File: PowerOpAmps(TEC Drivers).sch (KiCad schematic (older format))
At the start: 23 parts, among them U301 OPA569AIDWPR, U302 OPA569AIDWPR

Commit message: pushing all changes and ports
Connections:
- net Output_of_2.5V_Reference renamed REFERENCE_2.5V
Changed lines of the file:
@@
 	1    0    0    -1
 $EndComp
-Text Label 1050 3600 0    50   ~ 0
-Output_of_2.5V_Reference
 Wire Wire Line
 	7500 5350 7600 5350
@@
 	2900 2200 3700 2200
 Wire Wire Line
-	1050 3600 3350 3600
+	1750 3600 3350 3600
 Text Label 1100 2500 0    50   ~ 0
 Enable_Signal_from_Arduino_D5
@@
 	0    1    -1   0
 $EndComp
-Text HLabel 9450 2700 2    50   Input ~ 0
-4.2V_Power_Supply
+Text GLabel 9450 2700 2    50   Input ~ 0
+4.2V
+Text GLabel 1750 3600 0    50   Input ~ 0
+REFERENCE_2.5V
 $EndSCHEMATC

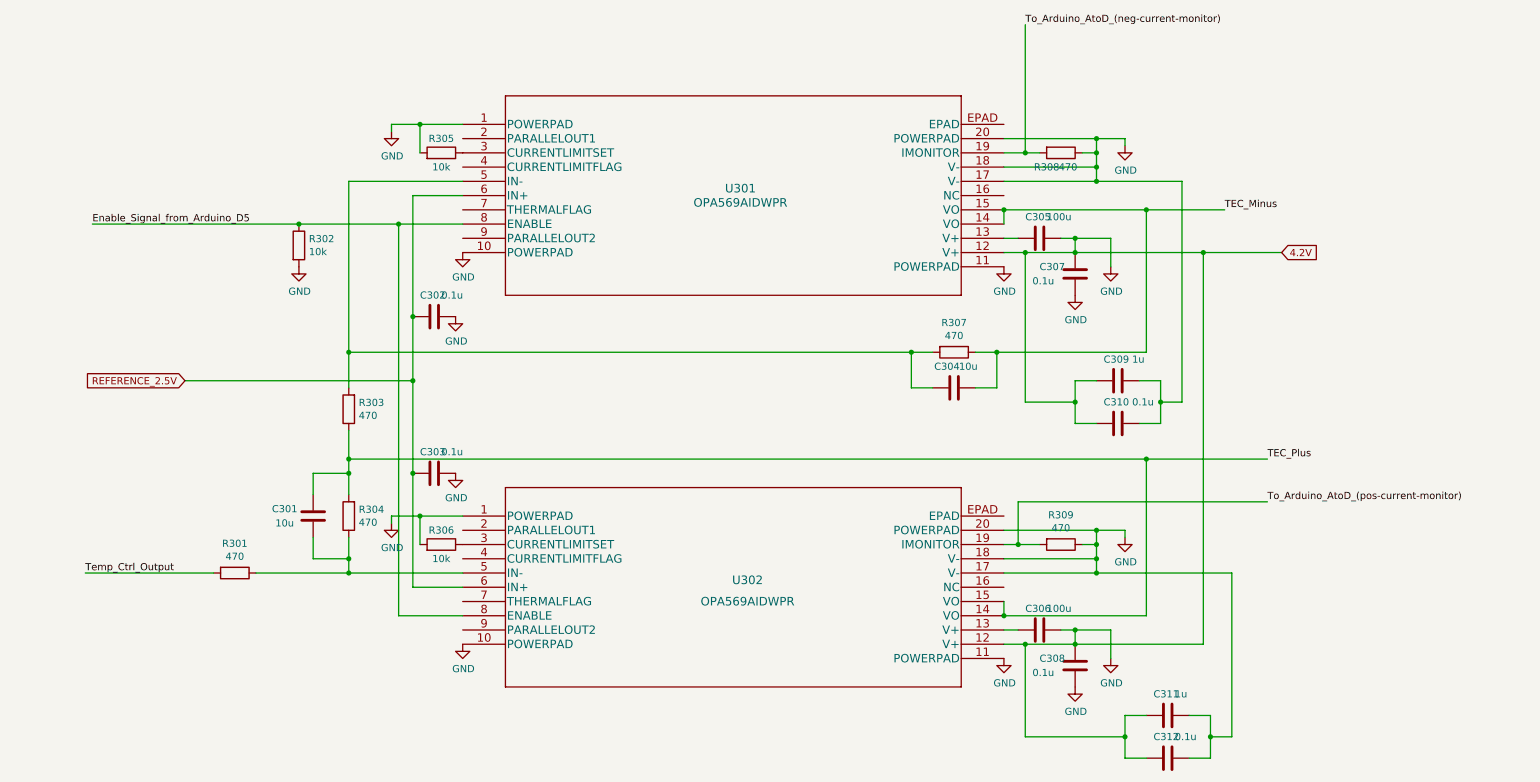
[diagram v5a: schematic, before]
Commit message: add thermal control output
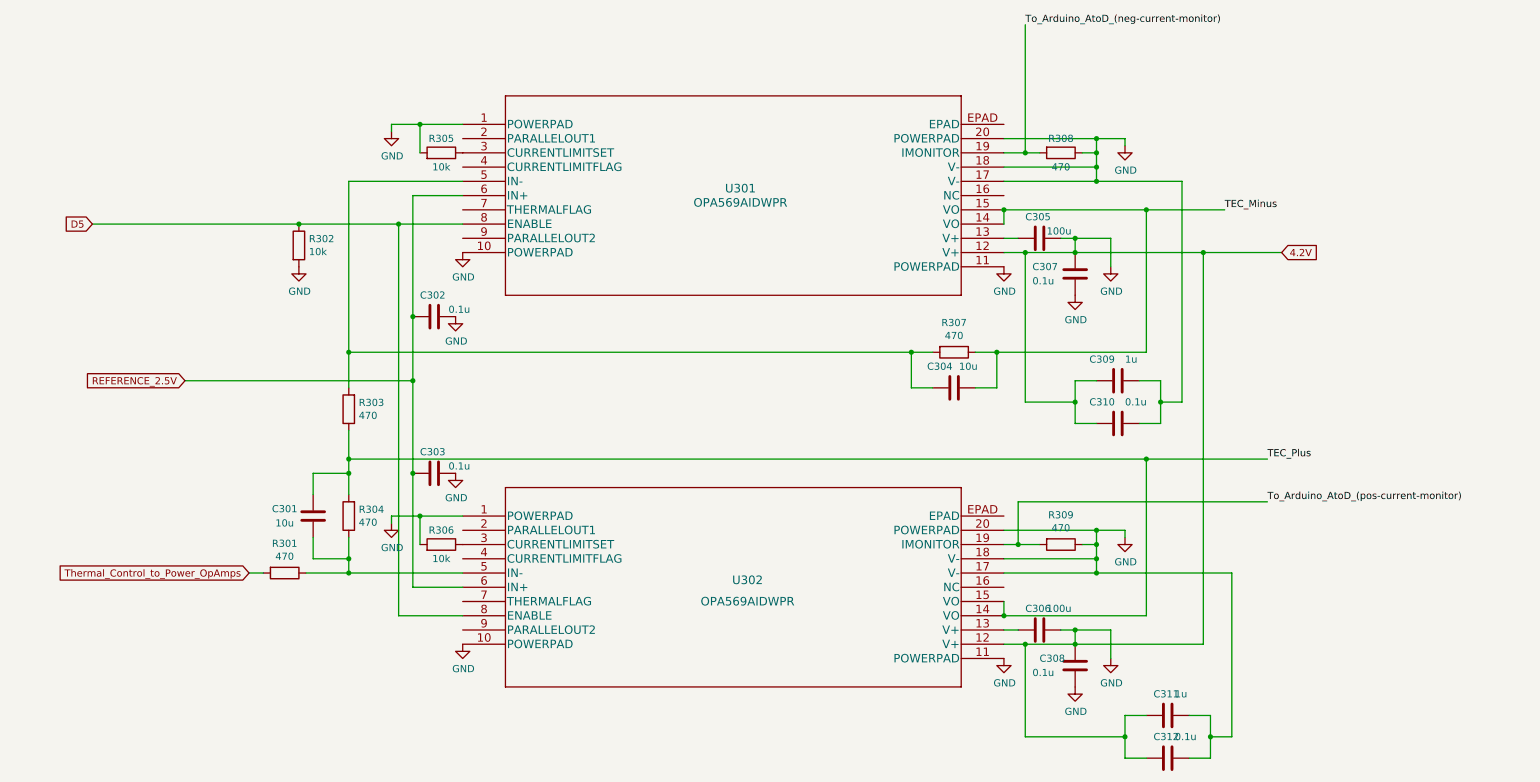
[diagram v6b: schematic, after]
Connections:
- net Enable_Signal_from_Arduino_D5 renamed D5
- net Temp_Ctrl_Output renamed Thermal_Control_to_Power_OpAmps
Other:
- moved on the sheet: R301
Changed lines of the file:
@@
 U 1 1 60C9D180
 P 7900 2000
-F 0 "R308" V 8000 1900 50  0000 C CNN
-F 1 "470" V 8000 2050 50  0000 C CNN
+F 0 "R308" V 7800 2000 50  0000 C CNN
+F 1 "470" V 8000 2000 50  0000 C CNN
 F 2 "Resistor_SMD:R_0402_1005Metric" V 7830 2000 50  0001 C CNN
 F 3 "~" H 7900 2000 50  0001 C CNN
@@
 U 1 1 60C9E72B
 P 8000 2850
-F 0 "C307" H 7750 2900 50  0000 L CNN
+F 0 "C307" H 7700 2900 50  0000 L CNN
 F 1 "0.1u" H 7700 2800 50  0000 L CNN
 F 2 "Capacitor_SMD:C_0402_1005Metric" H 8038 2700 50  0001 C CNN
@@
 P 7750 2600
 F 0 "C305" V 7600 2500 50  0000 L CNN
-F 1 "100u" V 7600 2650 50  0000 L CNN
+F 1 "100u" V 7700 2650 50  0000 L CNN
 F 2 "Capacitor_SMD:C_0402_1005Metric" H 7788 2450 50  0001 C CNN
 F 3 "~" H 7750 2600 50  0001 C CNN
@@
 U 1 1 60CADB61
 P 7150 3650
-F 0 "C304" V 7000 3600 50  0000 C CNN
+F 0 "C304" V 7000 3550 50  0000 C CNN
 F 1 "10u" V 7000 3750 50  0000 C CNN
 F 2 "Capacitor_SMD:C_0402_1005Metric" H 7188 3500 50  0001 C CNN
@@
 Wire Wire Line
 	2900 4850 2900 4950
-Wire Wire Line
-	2900 4950 2250 4950
-Connection ~ 2900 4950
 $Comp
 L Device:R R301
 U 1 1 60CB799D
-P 2100 4950
-F 0 "R301" V 1893 4950 50  0000 C CNN
-F 1 "470" V 1984 4950 50  0000 C CNN
-F 2 "Resistor_SMD:R_0402_1005Metric" V 2030 4950 50  0001 C CNN
-F 3 "~" H 2100 4950 50  0001 C CNN
-	1    2100 4950
-	0    1    1    0
-$EndComp
-Wire Wire Line
-	1950 4950 1050 4950
-Text Label 1050 4950 0    50   ~ 0
-Temp_Ctrl_Output
+P 2450 4950
+F 0 "R301" V 2243 4950 50  0000 C CNN
+F 1 "470" V 2334 4950 50  0000 C CNN
+F 2 "Resistor_SMD:R_0402_1005Metric" V 2380 4950 50  0001 C CNN
+F 3 "~" H 2450 4950 50  0001 C CNN
+	1    2450 4950
+	0    1    1    0
+$EndComp
 Wire Wire Line
 	3350 2300 3350 3150
@@
 P 3500 3150
 F 0 "C302" V 3350 3050 50  0000 L CNN
-F 1 "0.1u" V 3350 3200 50  0000 L CNN
+F 1 "0.1u" V 3450 3250 50  0000 L CNN
 F 2 "Capacitor_SMD:C_0402_1005Metric" H 3538 3000 50  0001 C CNN
 F 3 "~" H 3500 3150 50  0001 C CNN
@@
 P 3500 4250
 F 0 "C303" V 3350 4150 50  0000 L CNN
-F 1 "0.1u" V 3350 4300 50  0000 L CNN
+F 1 "0.1u" V 3450 4350 50  0000 L CNN
 F 2 "Capacitor_SMD:C_0402_1005Metric" H 3538 4100 50  0001 C CNN
 F 3 "~" H 3500 4250 50  0001 C CNN
@@
 Wire Wire Line
 	1750 3600 3350 3600
-Text Label 1100 2500 0    50   ~ 0
-Enable_Signal_from_Arduino_D5
 $Comp
 L Device:R R302
@@
 U 1 1 60CDE792
 P 8300 3600
-F 0 "C309" V 8150 3500 50  0000 L CNN
-F 1 "1u" V 8150 3700 50  0000 L CNN
+F 0 "C309" V 8150 3400 50  0000 L CNN
+F 1 "1u" V 8150 3650 50  0000 L CNN
 F 2 "Capacitor_SMD:C_0402_1005Metric" H 8338 3450 50  0001 C CNN
 F 3 "~" H 8300 3600 50  0001 C CNN
@@
 U 1 1 60CDE79C
 P 8300 3900
-F 0 "C310" V 8150 3800 50  0000 L CNN
-F 1 "0.1u" V 8150 4000 50  0000 L CNN
+F 0 "C310" V 8150 3700 50  0000 L CNN
+F 1 "0.1u" V 8150 3950 50  0000 L CNN
 F 2 "Capacitor_SMD:C_0402_1005Metric" H 8338 3750 50  0001 C CNN
 F 3 "~" H 8300 3900 50  0001 C CNN
@@
 Text GLabel 1750 3600 0    50   Input ~ 0
 REFERENCE_2.5V
+Text GLabel 1100 2500 0    50   Input ~ 0
+D5
+Text GLabel 2200 4950 0    50   Input ~ 0
+Thermal_Control_to_Power_OpAmps
+Wire Wire Line
+	2900 4950 2600 4950
+Connection ~ 2900 4950
+Wire Wire Line
+	2300 4950 2200 4950
 $EndSCHEMATC

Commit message: adding some more labels
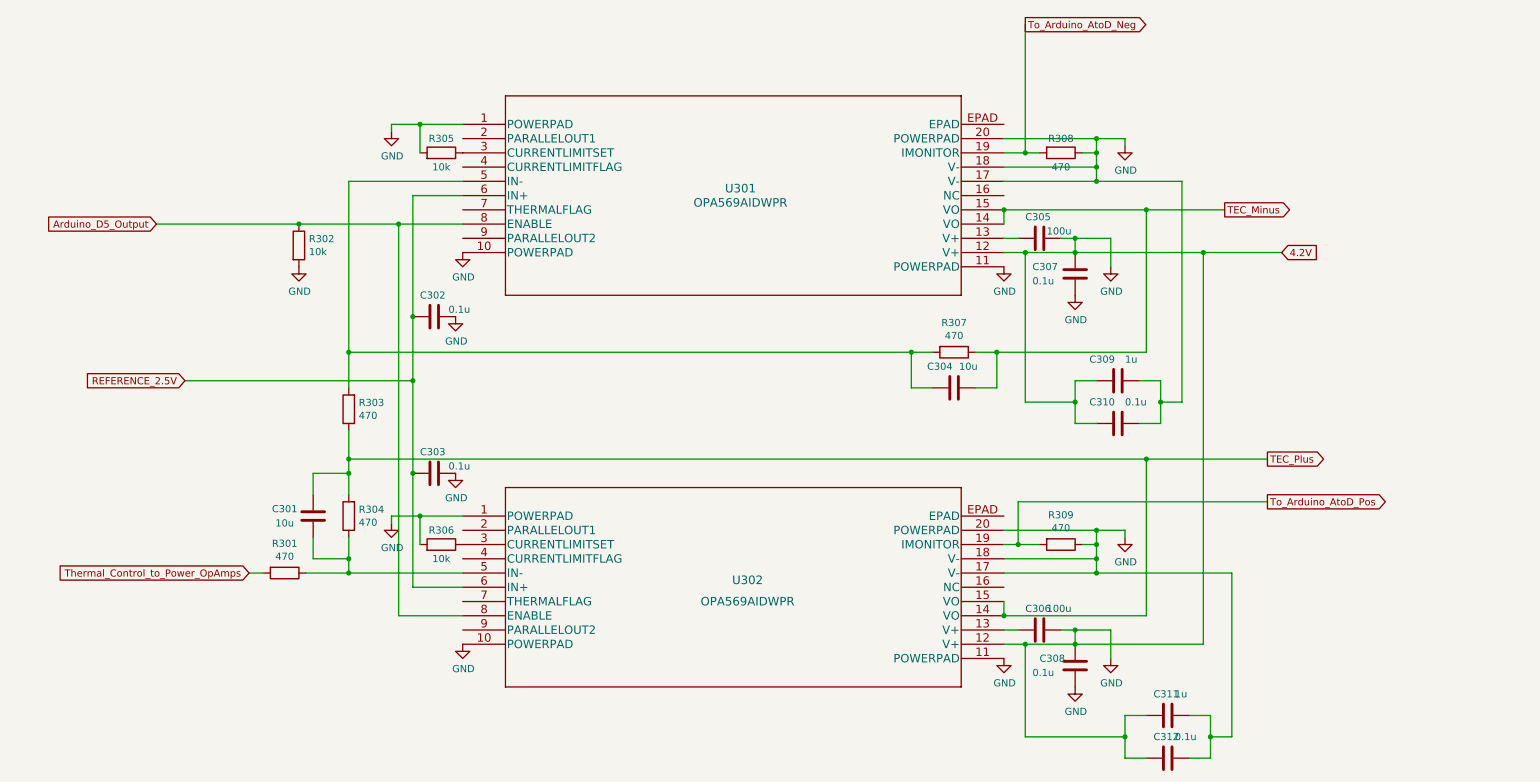
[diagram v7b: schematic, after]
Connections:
- net D5 renamed Arduino_D5_Output
- net To_Arduino_AtoD_(neg-current-monitor) renamed To_Arduino_AtoD_Neg
- net To_Arduino_AtoD_(pos-current-monitor) renamed To_Arduino_AtoD_Pos
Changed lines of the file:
@@
 Wire Wire Line
 	7500 2400 8500 2400
-Text Label 7650 1100 0    50   ~ 0
-To_Arduino_AtoD_(neg-current-monitor)
-Text Label 9050 2400 0    50   ~ 0
-TEC_Minus
 Wire Wire Line
 	8500 2400 8500 3400
@@
 Wire Wire Line
 	8500 2400 9050 2400
-Text Label 9350 4150 0    50   ~ 0
-TEC_Plus
 Wire Wire Line
 	8150 4950 8150 4850
@@
 Wire Wire Line
 	7600 4750 7750 4750
-Text Label 9350 4450 0    50   ~ 0
-To_Arduino_AtoD_(pos-current-monitor)
 Wire Wire Line
 	8500 5250 8500 4150
@@
 Connection ~ 2550 2500
 Wire Wire Line
-	2550 2500 1100 2500
+	2550 2500 1550 2500
 $Comp
 L power:GND #PWR0301
@@
 Text GLabel 1750 3600 0    50   Input ~ 0
 REFERENCE_2.5V
-Text GLabel 1100 2500 0    50   Input ~ 0
-D5
+Text GLabel 1550 2500 0    50   Input ~ 0
+Arduino_D5_Output
 Text GLabel 2200 4950 0    50   Input ~ 0
 Thermal_Control_to_Power_OpAmps
@@
 Wire Wire Line
 	2300 4950 2200 4950
+Text GLabel 9350 4150 2    50   Output ~ 0
+TEC_Plus
+Text GLabel 9050 2400 2    50   Output ~ 0
+TEC_Minus
+Text GLabel 9350 4450 2    50   Output ~ 0
+To_Arduino_AtoD_Pos
+Text GLabel 7650 1100 2    50   Output ~ 0
+To_Arduino_AtoD_Neg
 $EndSCHEMATC
